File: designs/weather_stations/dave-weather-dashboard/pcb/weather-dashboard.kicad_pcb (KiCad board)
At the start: 2 copper layers, 44 x 64 mm, 6 parts, among them SW2 SW_Omron_B3FS, U1 WEMOS_S2_Mini, U4 TFT_ST7735_SD

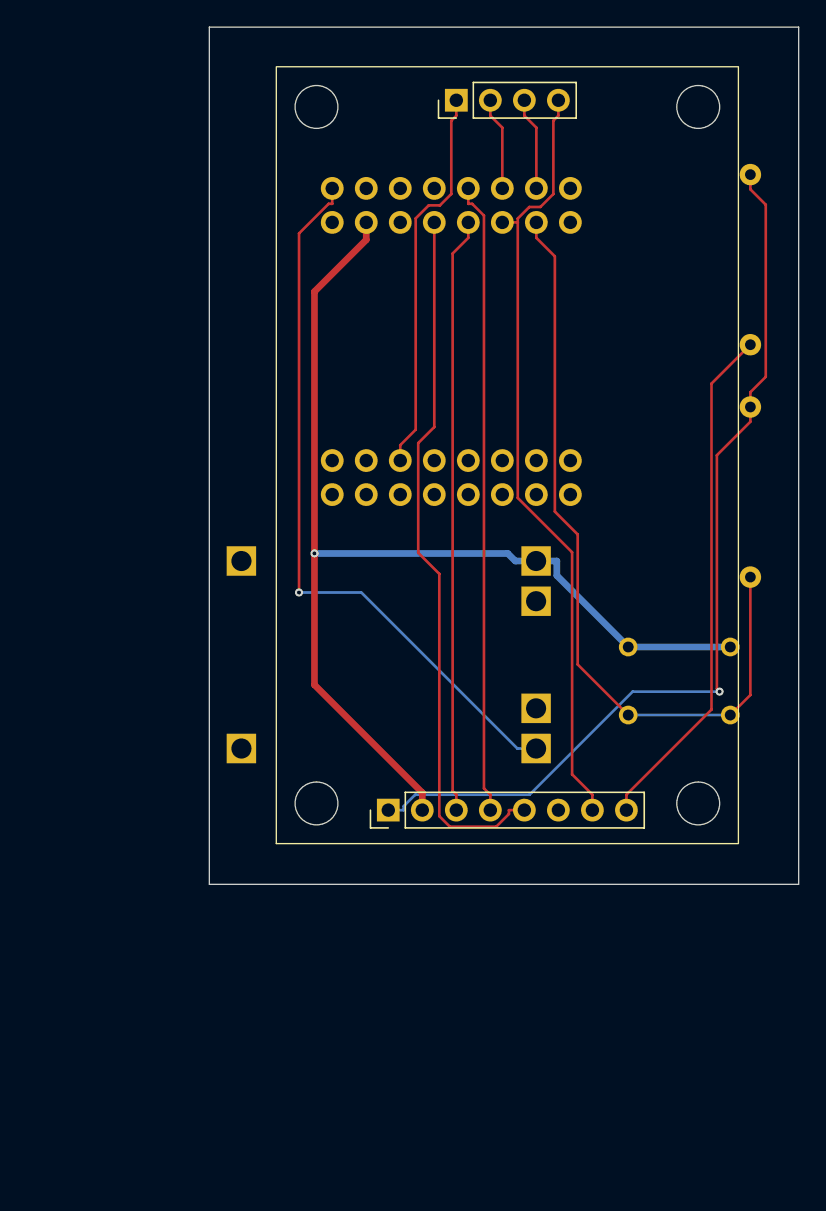
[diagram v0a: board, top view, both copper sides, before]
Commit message: Removed external resistor to use internal resistor and added load sharing circuit along with updated casing
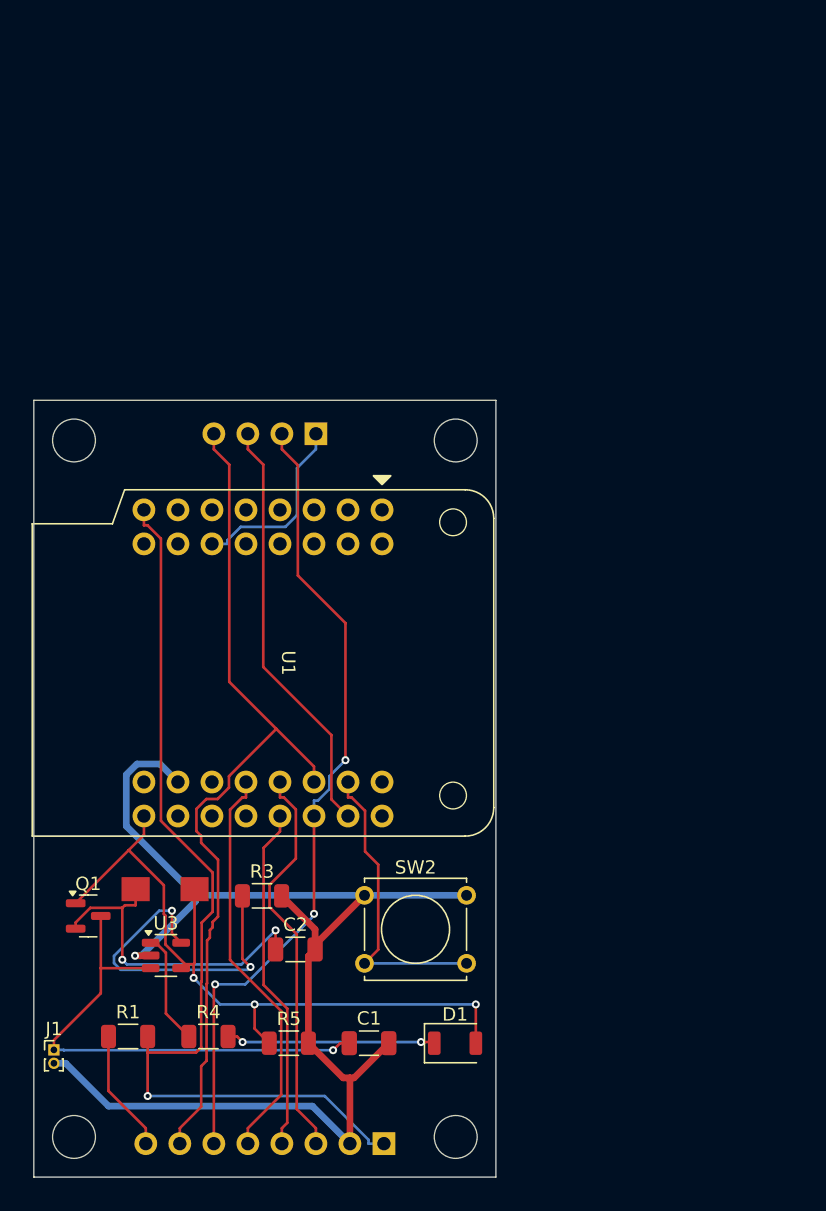
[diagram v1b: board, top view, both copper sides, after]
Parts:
- removed R2: 10k, Resistor_THT:R_Axial_DIN0309_L9.0mm_D3.2mm_P12.70mm_Horizontal
- removed U2: ~, asylum-weather:TP4056
- added C1: C1, Capacitor_SMD:C_1206_3216Metric, F.Cu at (162.5, 114.0)
- added C2: C2, Capacitor_SMD:C_1206_3216Metric, F.Cu at (157.0, 107.0)
- added D1: ORANGE, LED_SMD:LED_1206_3216Metric_ReverseMount_Hole1.8x2.4mm, F.Cu at (168.9, 114.0)
- added D2: D_Schottky, kicad-libraries:DO-214AC, F.Cu at (147.3, 102.5)
- added J1: Conn_01x02_MountingPin, Connector_PinHeader_1.00mm:PinHeader_1x02_P1.00mm_Vertical, F.Cu at (139.0, 114.5)
- added Q1: SL2301S, Package_TO_SOT_SMD:SOT-23, F.Cu at (141.6, 104.5)
- added R3: 50k, Resistor_SMD:R_1206_3216Metric, F.Cu at (154.5, 103.0)
- added R4: 1k, Resistor_SMD:R_1206_3216Metric, F.Cu at (150.5, 113.5)
- added R5: 100k, Resistor_SMD:R_1206_3216Metric, F.Cu at (156.5, 114.0)
- added U3: MCP73831-2-OT, Package_TO_SOT_SMD:SOT-23-5, F.Cu at (147.4, 107.5)
- R1: value 10 -> R1; footprint Resistor_THT:R_Axial_DIN0309_L9.0mm_D3.2mm_P12.70mm_Horizontal -> Resistor_SMD:R_1206_3216Metric; moved to F.Cu
- SW2, U1: moved to F.Cu
- U4: value TFT_ST7735_SD -> U4; moved to B.Cu
- moved R1 69.5 mm to (144.5, 113.5), turned to 0 degrees
- moved SW2 33.0 mm to (162.2, 103.0), turned to 0 degrees
- moved U4 30.5 mm to (155.0, 101.5)
- moved U1 27.8 mm to (156.0, 85.6), turned to -90 degrees
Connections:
- U1 pad 8: +5V -> +3V3
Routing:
- net MOSI: track 6.95 -> 60.5 mm, vias 0 -> 3
- net +BATT: track 0.00 -> 37.5 mm, vias 0 -> 1
- net Button: track 58.2 -> 22.7 mm
- net Net-(U4-LED): track 38.6 -> 9.15 mm
- net VCC: track 0.00 -> 25.2 mm, vias 0 -> 2
- net Net-(U3-PROG): track 0.00 -> 25.0 mm, vias 0 -> 2
- net MISO: track 6.95 -> 31.6 mm
- net TFT_DC: track 52.8 -> 30.3 mm
- net TFT_EN: track 47.3 -> 25.9 mm
- net GND: track 83.4 -> 99.4 mm
- net Net-(D1-K): track 0.00 -> 15.6 mm, vias 0 -> 2
- net SD_CS: track 29.1 -> 14.1 mm
- net TFT_CS: track 44.5 -> 29.9 mm
- net Net-(U3-STAT): track 0.00 -> 8.41 mm
- net SCK: track 58.2 -> 64.9 mm
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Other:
- board size 44 x 64 mm -> 34.5 x 58 mm

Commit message: done :)
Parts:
- moved D1 0.95 mm to (168.0, 114.0)
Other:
- board size 34.5 x 58 mm -> 35.5 x 59 mm

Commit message: screenshots
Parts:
- removed Q1: SL2301S, Package_TO_SOT_SMD:SOT-23
- added Q2: AO3401A, Package_TO_SOT_SMD:SOT-23, F.Cu at (141.6, 104.5)
- C1: value C1 -> 10uF; footprint Capacitor_SMD:C_1206_3216Metric -> Capacitor_SMD:C_0603_1608Metric
- C2: value C2 -> 10uF; footprint Capacitor_SMD:C_1206_3216Metric -> Capacitor_SMD:C_0603_1608Metric
- R1: value R1 -> 10
- U4: value U4 -> TFT_ST7735_SD
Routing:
- net GND: track 99.4 -> 103.4 mm
- net VBUS: track 54.7 -> 56.6 mm
- net VCC: track 24.9 -> 26.1 mm
- net +BATT: track 37.5 -> 38.2 mm
